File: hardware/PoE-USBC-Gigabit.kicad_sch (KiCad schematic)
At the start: 0 parts

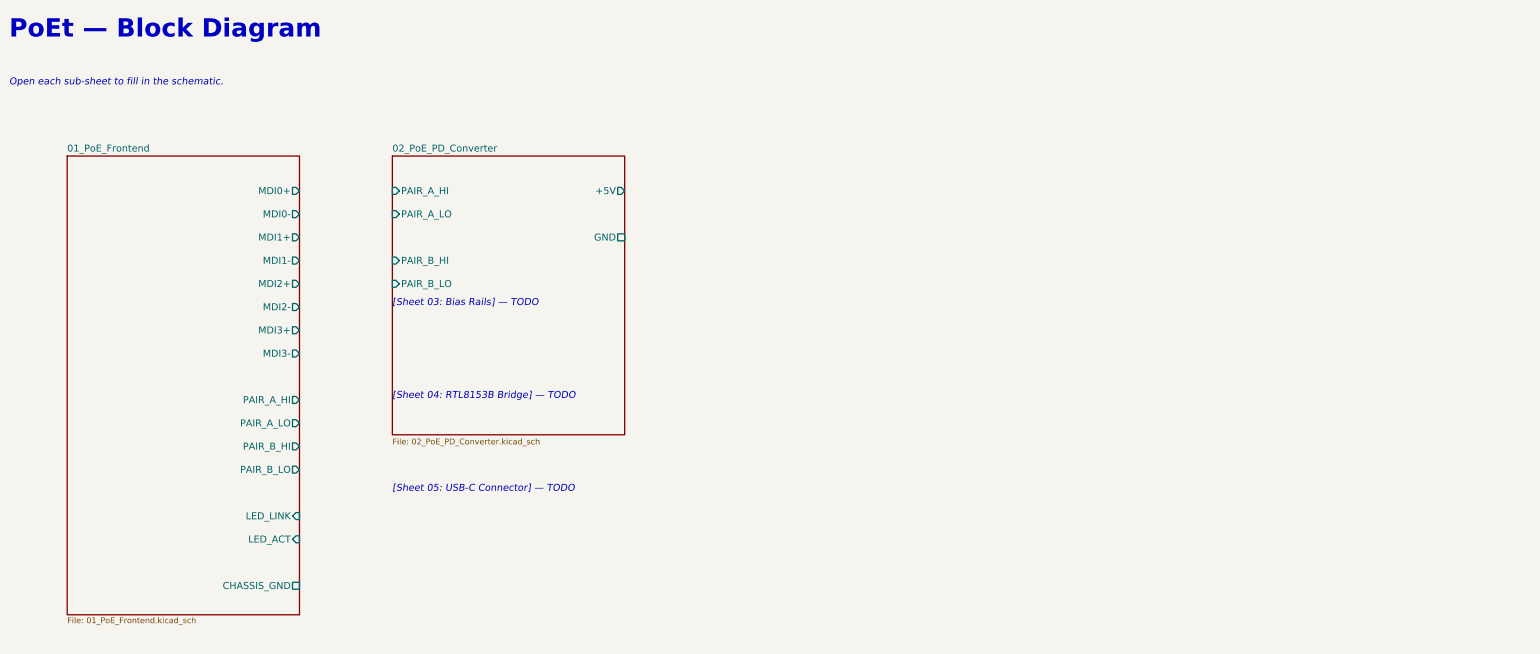
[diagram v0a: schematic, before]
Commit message: Add starter schematics for Sheets 03, 04, and 05
Each file follows the same pattern as the existing Sheet 01/02 starters:
all hierarchical labels pre-positioned on the correct edges, component
placement notes and pin mapping embedded as text annotations, and route
notes at the bottom. No actual symbols placed yet.

Sheet 03 (Bias Rails): +5V/GND in, +3V3/+1V0 out; U4 AP2112K-3.3 and
U5 RT9013-10GB LDOs; PWR_FLAG placement note.

Sheet 04 (RTL8153B Bridge): 4 power + 8 MDI inputs; 6 USB SS + 2 LED
outputs; U2 RTL8153B, U3 93C46 EEPROM, Y1 25 MHz xtal, SW1 reset.

Sheet 05 (USB-C Connector): 8 inputs (power + USB signals), no outputs;
J2 receptacle, R10/R11 CC pull-ups, U9 ESD, C15/C16 AC-coupling,
F1 PPTC, C11-C14 VBUS bulk; full 24-pin connector map in annotation.

Root schematic: replaced the three TODO text placeholders with proper
sheet symbols carrying fully-typed hierarchical pins on the correct
edges, placed to the right of Sheets 01/02 at pages 4-6.

Co-Authored-By: Claude Sonnet 4.6 <noreply@anthropic.com>
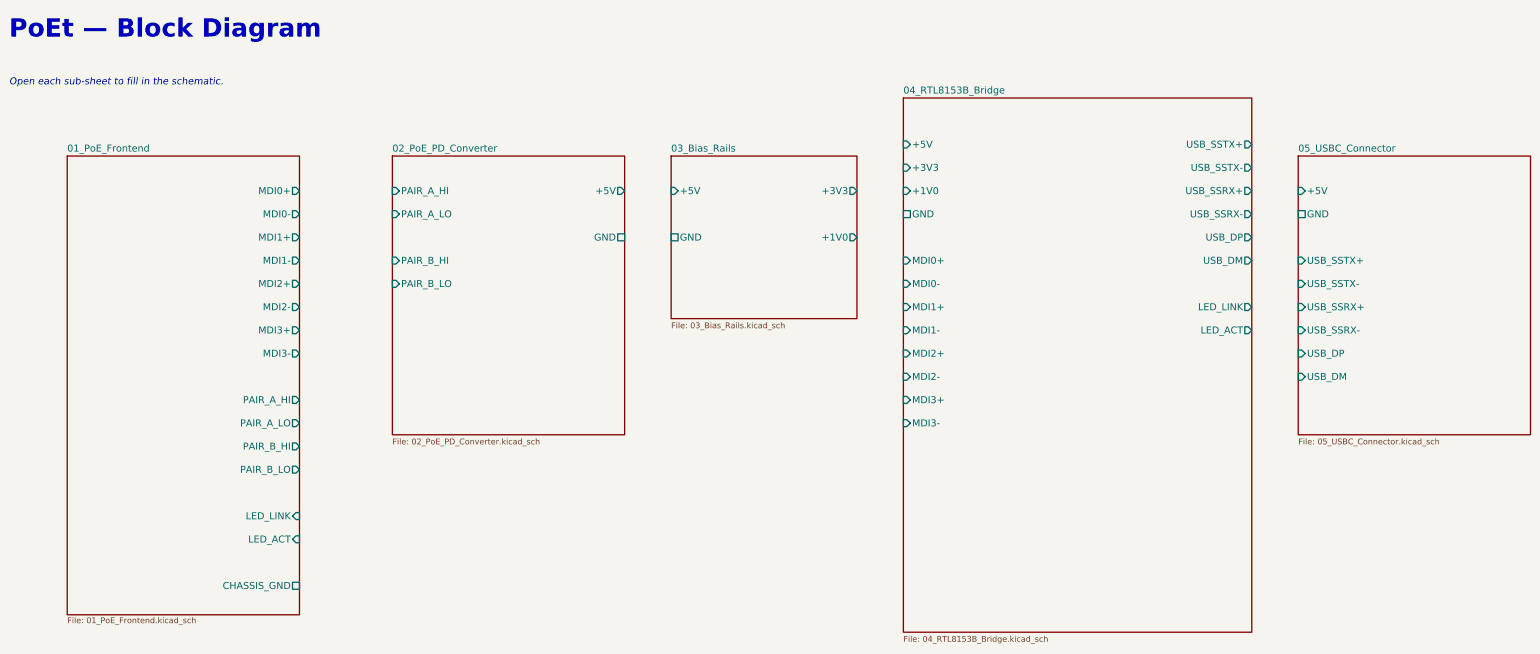
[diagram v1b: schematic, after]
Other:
- added sheet 03_Bias_Rails (03_Bias_Rails.kicad_sch)
- added sheet 04_RTL8153B_Bridge (04_RTL8153B_Bridge.kicad_sch)
- added sheet 05_USBC_Connector (05_USBC_Connector.kicad_sch)
- note removed: "[Sheet 03: Bias Rails] — TODO"
- note removed: "[Sheet 04: RTL8153B Bridge] — TODO"
- note removed: "[Sheet 05: USB-C Connector] — TODO"
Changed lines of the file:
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@@
 		)
 	)
-	(text "[Sheet 03: Bias Rails] — TODO"
+	(sheet
+		(at 170.18 38.1)
+		(size 40.64 35.56)
 		(exclude_from_sim no)
-		(at 109.22 71.12 0)
-		(effects (font (size 1.524 1.524) italic) (justify left bottom))
+		(in_bom yes)
+		(on_board yes)
+		(dnp no)
+		(fields_autoplaced yes)
+		(stroke (width 0.1524) (type solid))
+		(fill (color 0 0 0 0.0000))
+		(property "Sheetname" "03_Bias_Rails"
+			(at 170.18 37.3104 0)
+			(effects (font (size 1.524 1.524)) (justify left bottom))
+		)
+		(property "Sheetfile" "03_Bias_Rails.kicad_sch"
+			(at 170.18 74.4314 0)
+			(effects (font (size 1.27 1.27)) (justify left top))
+		)
+		(pin "+5V" input (at 170.18 45.72 180)
+			(effects (font (size 1.524 1.524)) (justify left))
+		)
+		(pin "GND" passive (at 170.18 55.88 180)
+			(effects (font (size 1.524 1.524)) (justify left))
+		)
+		(pin "+3V3" output (at 210.82 45.72 0)
+			(effects (font (size 1.524 1.524)) (justify right))
+		)
+		(pin "+1V0" output (at 210.82 55.88 0)
+			(effects (font (size 1.524 1.524)) (justify right))
+		)
+		(instances
+			(project "PoE-USBC-Gigabit"
+				(path "/00000000-0000-0000-0000-000000000001"
+					(page "4")
+				)
+			)
+		)
 	)
-	(text "[Sheet 04: RTL8153B Bridge] — TODO"
+	(sheet
+		(at 220.98 25.4)
+		(size 76.2 116.84)
 		(exclude_from_sim no)
-		(at 109.22 91.44 0)
-		(effects (font (size 1.524 1.524) italic) (justify left bottom))
+		(in_bom yes)
+		(on_board yes)
+		(dnp no)
+		(fields_autoplaced yes)
+		(stroke (width 0.1524) (type solid))
+		(fill (color 0 0 0 0.0000))
+		(property "Sheetname" "04_RTL8153B_Bridge"
+			(at 220.98 24.6104 0)
+			(effects (font (size 1.524 1.524)) (justify left bottom))
+		)
+		(property "Sheetfile" "04_RTL8153B_Bridge.kicad_sch"
+			(at 220.98 143.0114 0)
+			(effects (font (size 1.27 1.27)) (justify left top))
+		)
+		(pin "+5V" input (at 220.98 35.56 180)
+			(effects (font (size 1.524 1.524)) (justify left))
+		)
+		(pin "+3V3" input (at 220.98 40.64 180)
+			(effects (font (size 1.524 1.524)) (justify left))
+		)
+		(pin "+1V0" input (at 220.98 45.72 180)
+			(effects (font (size 1.524 1.524)) (justify left))
+		)
+		(pin "GND" passive (at 220.98 50.8 180)
+			(effects (font (size 1.524 1.524)) (justify left))
+		)
+		(pin "MDI0+" input (at 220.98 60.96 180)
+			(effects (font (size 1.524 1.524)) (justify left))
+		)
+		(pin "MDI0-" input (at 220.98 66.04 180)
+			(effects (font (size 1.524 1.524)) (justify left))
+		)
+		(pin "MDI1+" input (at 220.98 71.12 180)
+			(effects (font (size 1.524 1.524)) (justify left))
+		)
+		(pin "MDI1-" input (at 220.98 76.2 180)
+			(effects (font (size 1.524 1.524)) (justify left))
+		)
+		(pin "MDI2+" input (at 220.98 81.28 180)
+			(effects (font (size 1.524 1.524)) (justify left))
+		)
+		(pin "MDI2-" input (at 220.98 86.36 180)
+			(effects (font (size 1.524 1.524)) (justify left))
+		)
+		(pin "MDI3+" input (at 220.98 91.44 180)
+			(effects (font (size 1.524 1.524)) (justify left))
+		)
+		(pin "MDI3-" input (at 220.98 96.52 180)
+			(effects (font (size 1.524 1.524)) (justify left))
+		)
+		(pin "USB_SSTX+" output (at 297.18 35.56 0)
+			(effects (font (size 1.524 1.524)) (justify right))
+		)
+		(pin "USB_SSTX-" output (at 297.18 40.64 0)
+			(effects (font (size 1.524 1.524)) (justify right))
+		)
+		(pin "USB_SSRX+" output (at 297.18 45.72 0)
+			(effects (font (size 1.524 1.524)) (justify right))
+		)
+		(pin "USB_SSRX-" output (at 297.18 50.8 0)
+			(effects (font (size 1.524 1.524)) (justify right))
+		)
+		(pin "USB_DP" output (at 297.18 55.88 0)
+			(effects (font (size 1.524 1.524)) (justify right))
+		)
+		(pin "USB_DM" output (at 297.18 60.96 0)
+			(effects (font (size 1.524 1.524)) (justify right))
+		)
+		(pin "LED_LINK" output (at 297.18 71.12 0)
+			(effects (font (size 1.524 1.524)) (justify right))
+		)
+		(pin "LED_ACT" output (at 297.18 76.2 0)
+			(effects (font (size 1.524 1.524)) (justify right))
+		)
+		(instances
+			(project "PoE-USBC-Gigabit"
+				(path "/00000000-0000-0000-0000-000000000001"
+					(page "5")
+				)
+			)
+		)
 	)
-	(text "[Sheet 05: USB-C Connector] — TODO"
+	(sheet
+		(at 307.34 38.1)
+		(size 50.8 60.96)
 		(exclude_from_sim no)
-		(at 109.22 111.76 0)
-		(effects (font (size 1.524 1.524) italic) (justify left bottom))
+		(in_bom yes)
+		(on_board yes)
+		(dnp no)
+		(fields_autoplaced yes)
+		(stroke (width 0.1524) (type solid))
+		(fill (color 0 0 0 0.0000))
+		(property "Sheetname" "05_USBC_Connector"
+			(at 307.34 37.3104 0)
+			(effects (font (size 1.524 1.524)) (justify left bottom))
+		)
+		(property "Sheetfile" "05_USBC_Connector.kicad_sch"
+			(at 307.34 99.8314 0)
+			(effects (font (size 1.27 1.27)) (justify left top))
+		)
+		(pin "+5V" input (at 307.34 45.72 180)
+			(effects (font (size 1.524 1.524)) (justify left))
+		)
+		(pin "GND" passive (at 307.34 50.8 180)
+			(effects (font (size 1.524 1.524)) (justify left))
+		)
+		(pin "USB_SSTX+" input (at 307.34 60.96 180)
+			(effects (font (size 1.524 1.524)) (justify left))
+		)
+		(pin "USB_SSTX-" input (at 307.34 66.04 180)
+			(effects (font (size 1.524 1.524)) (justify left))
+		)
+		(pin "USB_SSRX+" input (at 307.34 71.12 180)
+			(effects (font (size 1.524 1.524)) (justify left))
+		)
+		(pin "USB_SSRX-" input (at 307.34 76.2 180)
+			(effects (font (size 1.524 1.524)) (justify left))
+		)
+		(pin "USB_DP" input (at 307.34 81.28 180)
+			(effects (font (size 1.524 1.524)) (justify left))
+		)
+		(pin "USB_DM" input (at 307.34 86.36 180)
+			(effects (font (size 1.524 1.524)) (justify left))
+		)
+		(instances
+			(project "PoE-USBC-Gigabit"
+				(path "/00000000-0000-0000-0000-000000000001"
+					(page "6")
+				)
+			)
+		)
 	)
 	(sheet_instances

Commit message: Add gh0stee.com branding to all title blocks and README
Added (company "gh0stee.com") to the KiCad title_block of all six
schematics (root + Sheets 01–05) and the PCB file so the company name
appears in every printed/exported title block. Added a byline link to
README.md below the project description.

Co-Authored-By: Claude Sonnet 4.6 <noreply@anthropic.com>
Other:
- company: (none) -> gh0stee.com
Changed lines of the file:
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@@
 		(date "2026-05-10")
 		(rev "A")
+		(company "gh0stee.com")
 		(comment 1 "Root sheet — hierarchical sub-sheets for each functional block")
 		(comment 2 "PoE 802.3af  →  Si3402-B  →  RTL8153B USB 3.0 / GbE  →  USB-C 5 V/2 A")
